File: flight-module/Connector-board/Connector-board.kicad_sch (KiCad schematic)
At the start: 15 parts, among them J2 Stack_Shape

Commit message: Commit - corrections from Dulanya
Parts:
- added D7, D8: D_Schottky, Diode_SMD:D_SOD-128, symbol Device:D_Schottky
- renumbered 4TC_DSUB to 4TC_DSUB1, GND_DSUB to GND_DSUB1, J2 to J1, PT_DSUB to PT_DSUB1, SOLENOIDS_DSUB to SOLENOIDS_DSUB1
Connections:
- net ETH_VENT: now also D7.1 (K)
- net GND: now also J1.B17 (Pin_17), J1.B5 (Pin_5), J1.B9 (Pin_9), D7.2 (A), D8.2 (A)
- net LOX_VENT: now also D8.1 (K)

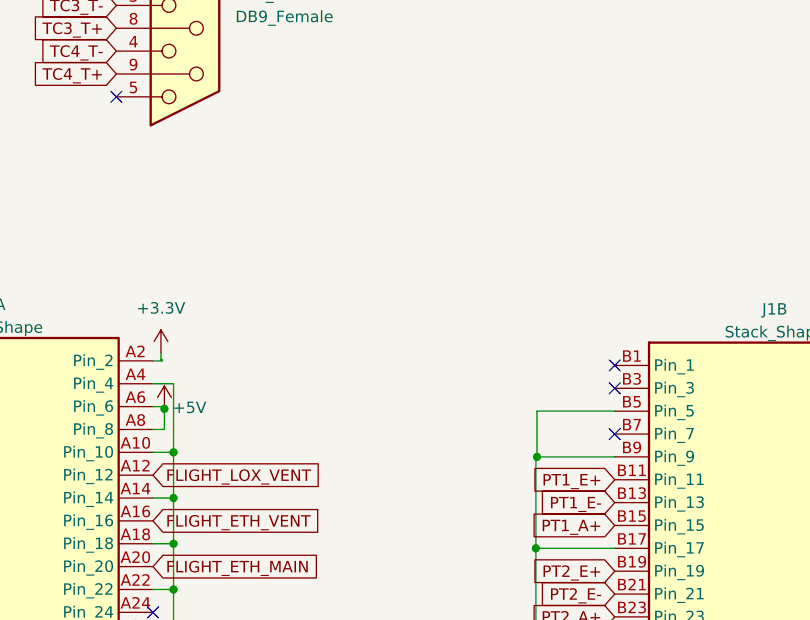
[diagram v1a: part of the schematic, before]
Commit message: connector fix - change to SMD
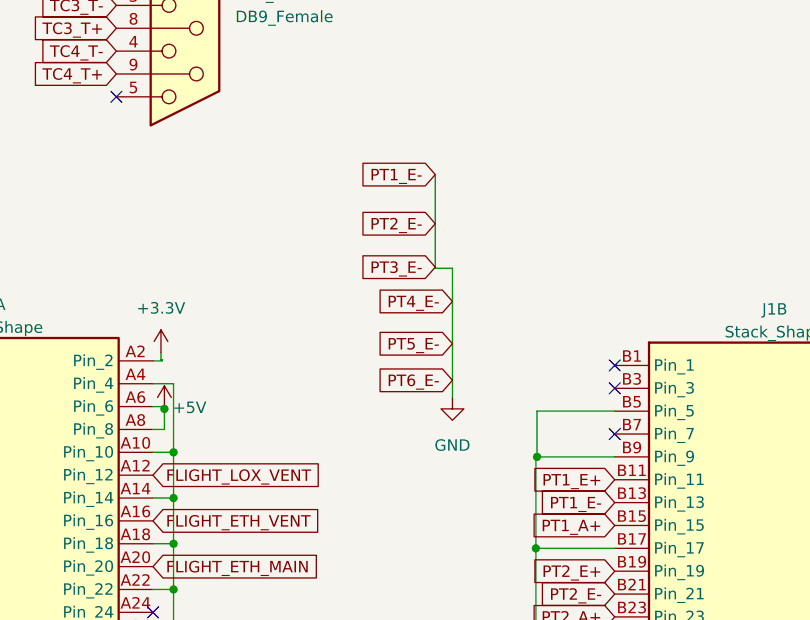
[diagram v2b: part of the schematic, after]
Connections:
- net PT1_E- is gone; now on net GND: J1.B13 (Pin_13), PT_DSUB1.2
- net PT2_E- is gone; now on net GND: J1.B21 (Pin_21), PT_DSUB1.4
- net PT3_E- is gone; now on net GND: J1.B29 (Pin_29), PT_DSUB1.6
- net PT4_E- is gone; now on net GND: J1.B37 (Pin_37), PT_DSUB1.8
- net PT5_E- is gone; now on net GND: J1.B30 (Pin_30), PT_DSUB1.10
- net PT6_E- is gone; now on net GND: J1.B38 (Pin_38), PT_DSUB1.12
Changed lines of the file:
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@@
+    (stroke (width 0) (type default))
+  )
+  (wire (pts (xy 104.775 123.825) (xy 106.68 123.825))
     (stroke (width 0) (type default))
   )
@@
     (stroke (width 0) (type default))
   )
+  (wire (pts (xy 104.775 123.825) (xy 104.775 113.411))
+    (stroke (width 0) (type default))
+  )
   (wire (pts (xy 32.893 144.272) (xy 32.893 144.526))
     (stroke (width 0) (type default))
@@
   )
   (wire (pts (xy 165.1 142.24) (xy 160.274 142.24))
+    (stroke (width 0) (type default))
+  )
+  (wire (pts (xy 106.68 123.825) (xy 106.68 138.176))
     (stroke (width 0) (type default))
   )
@@
     )
   )
+  (global_label "PT3_E-" (shape input) (at 104.775 123.698 180) (fields_autoplaced)
+    (effects (font (size 1.27 1.27)) (justify right))
+    (property "Intersheetrefs" "${INTERSHEET_REFS}" (at 94.6537 123.698 0)
+      (effects (font (size 1.27 1.27)) (justify right) hide)
+    )
+  )
   (global_label "FLIGHT_ETH_VENT" (shape input) (at 37.846 151.892 180) (fields_autoplaced)
     (effects (font (size 1.27 1.27)) (justify right))
@@
     )
   )
+  (global_label "PT1_E-" (shape input) (at 104.775 113.411 180) (fields_autoplaced)
+    (effects (font (size 1.27 1.27)) (justify right))
+    (property "Intersheetrefs" "${INTERSHEET_REFS}" (at 94.6537 113.411 0)
+      (effects (font (size 1.27 1.27)) (justify right) hide)
+    )
+  )
   (global_label "PT6_A+" (shape input) (at 99.06 80.01 180) (fields_autoplaced)
     (effects (font (size 1.27 1.27)) (justify right))
@@
     )
   )
+  (global_label "PT5_E-" (shape input) (at 106.68 132.207 180) (fields_autoplaced)
+    (effects (font (size 1.27 1.27)) (justify right))
+    (property "Intersheetrefs" "${INTERSHEET_REFS}" (at 96.5587 132.207 0)
+      (effects (font (size 1.27 1.27)) (justify right) hide)
+    )
+  )
   (global_label "SPI_MISO" (shape input) (at 246.888 28.448 0) (fields_autoplaced)
     (effects (font (size 1.27 1.27)) (justify left))
@@
     )
   )
+  (global_label "PT6_E-" (shape input) (at 106.68 136.271 180) (fields_autoplaced)
+    (effects (font (size 1.27 1.27)) (justify right))
+    (property "Intersheetrefs" "${INTERSHEET_REFS}" (at 96.5587 136.271 0)
+      (effects (font (size 1.27 1.27)) (justify right) hide)
+    )
+  )
   (global_label "PT1_A+" (shape input) (at 124.714 152.4 180) (fields_autoplaced)
     (effects (font (size 1.27 1.27)) (justify right))
@@
     )
   )
+  (global_label "PT4_E-" (shape input) (at 106.68 127.508 180) (fields_autoplaced)
+    (effects (font (size 1.27 1.27)) (justify right))
+    (property "Intersheetrefs" "${INTERSHEET_REFS}" (at 96.5587 127.508 0)
+      (effects (font (size 1.27 1.27)) (justify right) hide)
+    )
+  )
   (global_label "PT4_E+" (shape input) (at 99.06 57.15 180) (fields_autoplaced)
     (effects (font (size 1.27 1.27)) (justify right))
@@
     (effects (font (size 1.27 1.27)) (justify right))
     (property "Intersheetrefs" "${INTERSHEET_REFS}" (at 38.6103 45.974 0)
+      (effects (font (size 1.27 1.27)) (justify right) hide)
+    )
+  )
+  (global_label "PT2_E-" (shape input) (at 104.775 118.872 180) (fields_autoplaced)
+    (effects (font (size 1.27 1.27)) (justify right))
+    (property "Intersheetrefs" "${INTERSHEET_REFS}" (at 94.6537 118.872 0)
       (effects (font (size 1.27 1.27)) (justify right) hide)
     )
@@
         )
       )
+    )
+  )
+  (symbol (lib_id "power:GND") (at 106.68 138.176 0) (unit 1)
+    (in_bom yes) (on_board yes) (dnp no) (fields_autoplaced)
+    (property "Reference" "#PWR034" (at 106.68 144.526 0)
+      (effects (font (size 1.27 1.27)) hide)
+    )
+    (property "Value" "GND" (at 106.68 143.51 0)
+      (effects (font (size 1.27 1.27)))
+    )
+    (property "Footprint" "" (at 106.68 138.176 0)
+      (effects (font (size 1.27 1.27)) hide)
+    )
+    (property "Datasheet" "" (at 106.68 138.176 0)
+      (effects (font (size 1.27 1.27)) hide)
+    )
+    (pin "1")
+    (instances
+      (project "Connector-board"
+        (path "/9e0a4b39-2b30-4bec-9684-92acf902e3a8"
+          (reference "#PWR034") (unit 1)
+        )
+      )

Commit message: connector gerbs
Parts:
- PT_DSUB1: footprint Connector_Dsub:DSUB-25_Male_Vertical_P2.77x2.84mm_MountingHoles -> Connector_Dsub:DSUB-25_Female_Vertical_P2.77x2.84mm_MountingHoles
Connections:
- net PT1_E+ is gone; now on net +5V: J1.B11 (Pin_11), PT_DSUB1.1
- net PT2_E+ is gone; now on net +5V: J1.B19 (Pin_19), PT_DSUB1.3
- net PT3_E+ is gone; now on net +5V: J1.B27 (Pin_27), PT_DSUB1.5
- net PT4_E+ is gone; now on net +5V: J1.B35 (Pin_35), PT_DSUB1.7
- net PT5_E+ is gone; now on net +5V: J1.B28 (Pin_28), PT_DSUB1.9
- net PT6_E+ is gone; now on net +5V: J1.B36 (Pin_36), PT_DSUB1.11
